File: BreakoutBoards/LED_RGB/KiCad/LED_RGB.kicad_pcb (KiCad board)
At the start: 2 copper layers, 11.3 x 12.8 mm, 6 parts, among them J1 HDR-TH_4P-P2.54-V-M

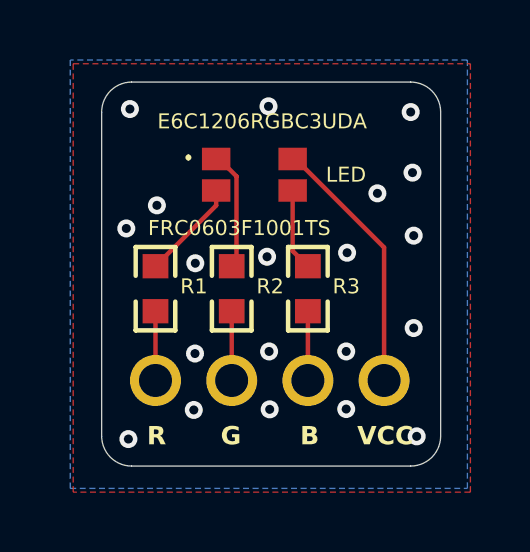
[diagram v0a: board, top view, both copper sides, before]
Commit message: removing resistors to make more versatile and selecting new led to use
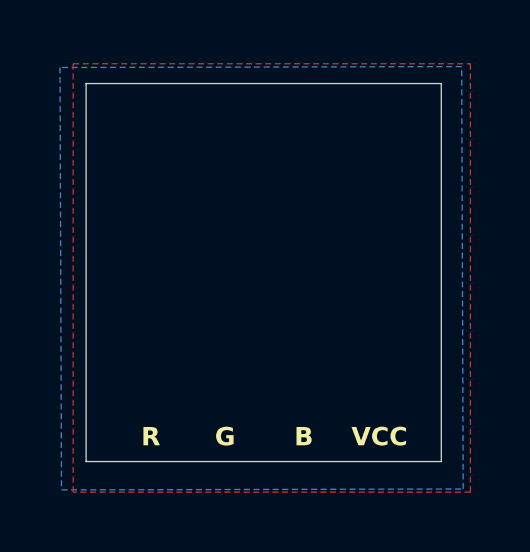
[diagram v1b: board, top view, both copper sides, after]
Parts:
- removed J1: HDR-TH_4P-P2.54-V-M, clectric-diy:HDR-TH_4P-P2.54-V-M
- removed LED1: E6C1206RGBC3UDA, clectric-diy:E6C1206RGBC3UDA
- removed R1, R2, R3: FRC0603F1001TS, clectric-diy:R0603
- moved G*** 0.20 mm to (94.7, 81.3)
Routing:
- net VCC: track 8.70 -> 0.00 mm
- net LED_GREEN: track 6.49 -> 0.00 mm
- net LED_RED: track 5.68 -> 0.00 mm
- net LED_BLUE: track 5.04 -> 0.00 mm
- net GND: vias 20 -> 0
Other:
- board size 11.3 x 12.8 mm -> 11.8 x 12.6 mm
- board text removed: "FRC0603F1001TS"
- board text removed: "LED"
